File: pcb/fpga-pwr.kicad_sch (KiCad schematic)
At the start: 6 parts, among them M1V0 TestPoint, M1V2 TestPoint, U5 XC7A35T-FGG484

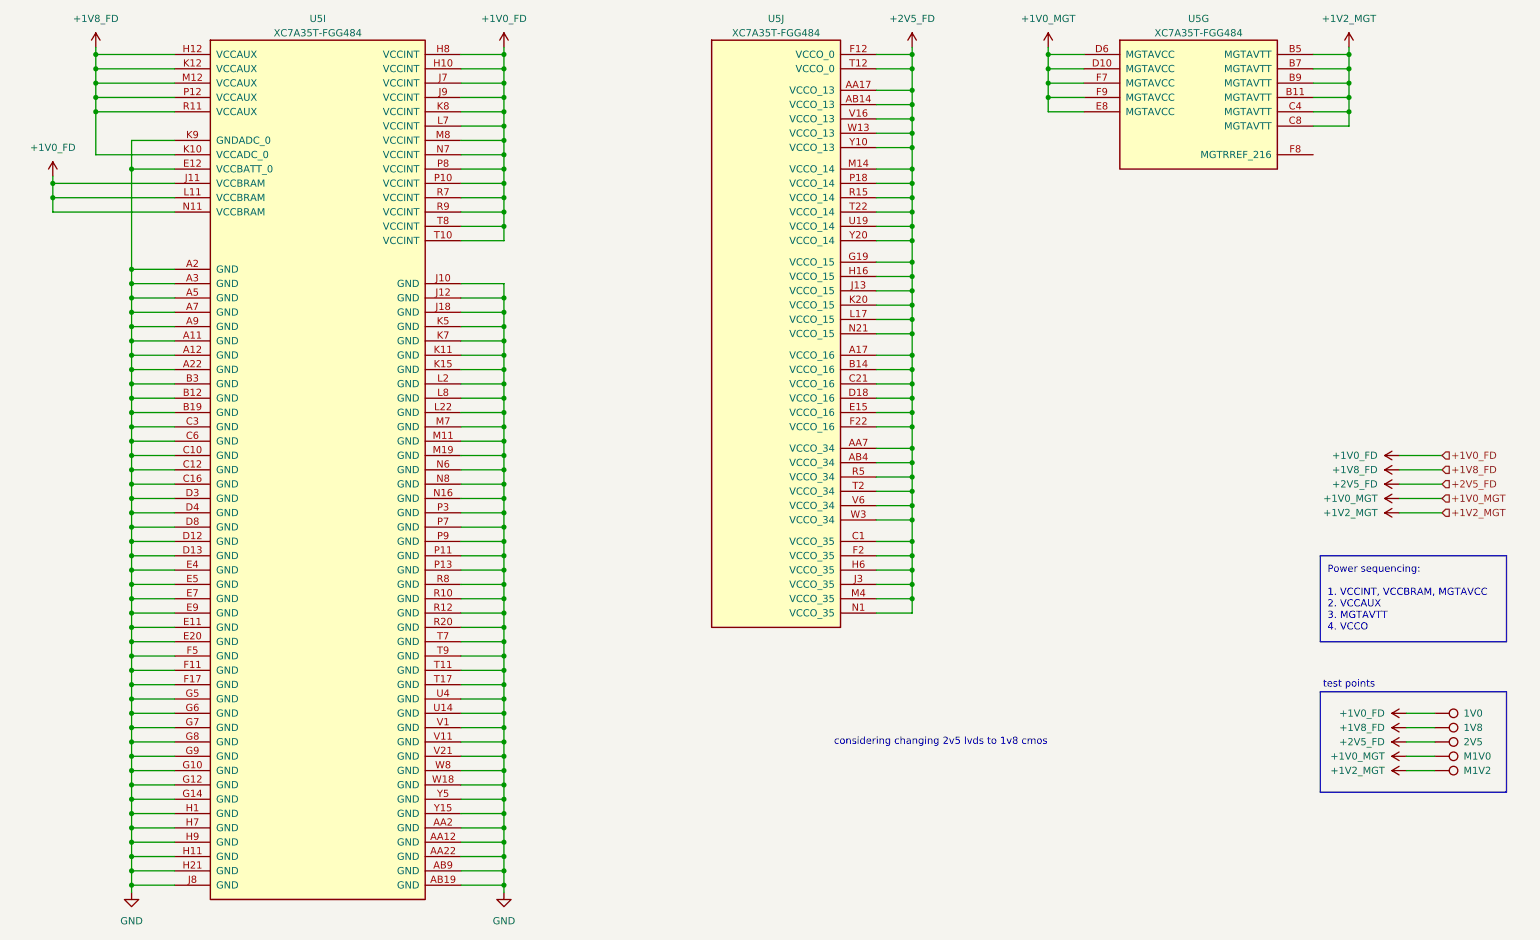
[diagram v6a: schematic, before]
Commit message: reorg hierarchical, define buses
added bus definitions, aliasing, reorganized sub-sheets for hierarchical interpretation, grouped fpga. pending dram and mram addition
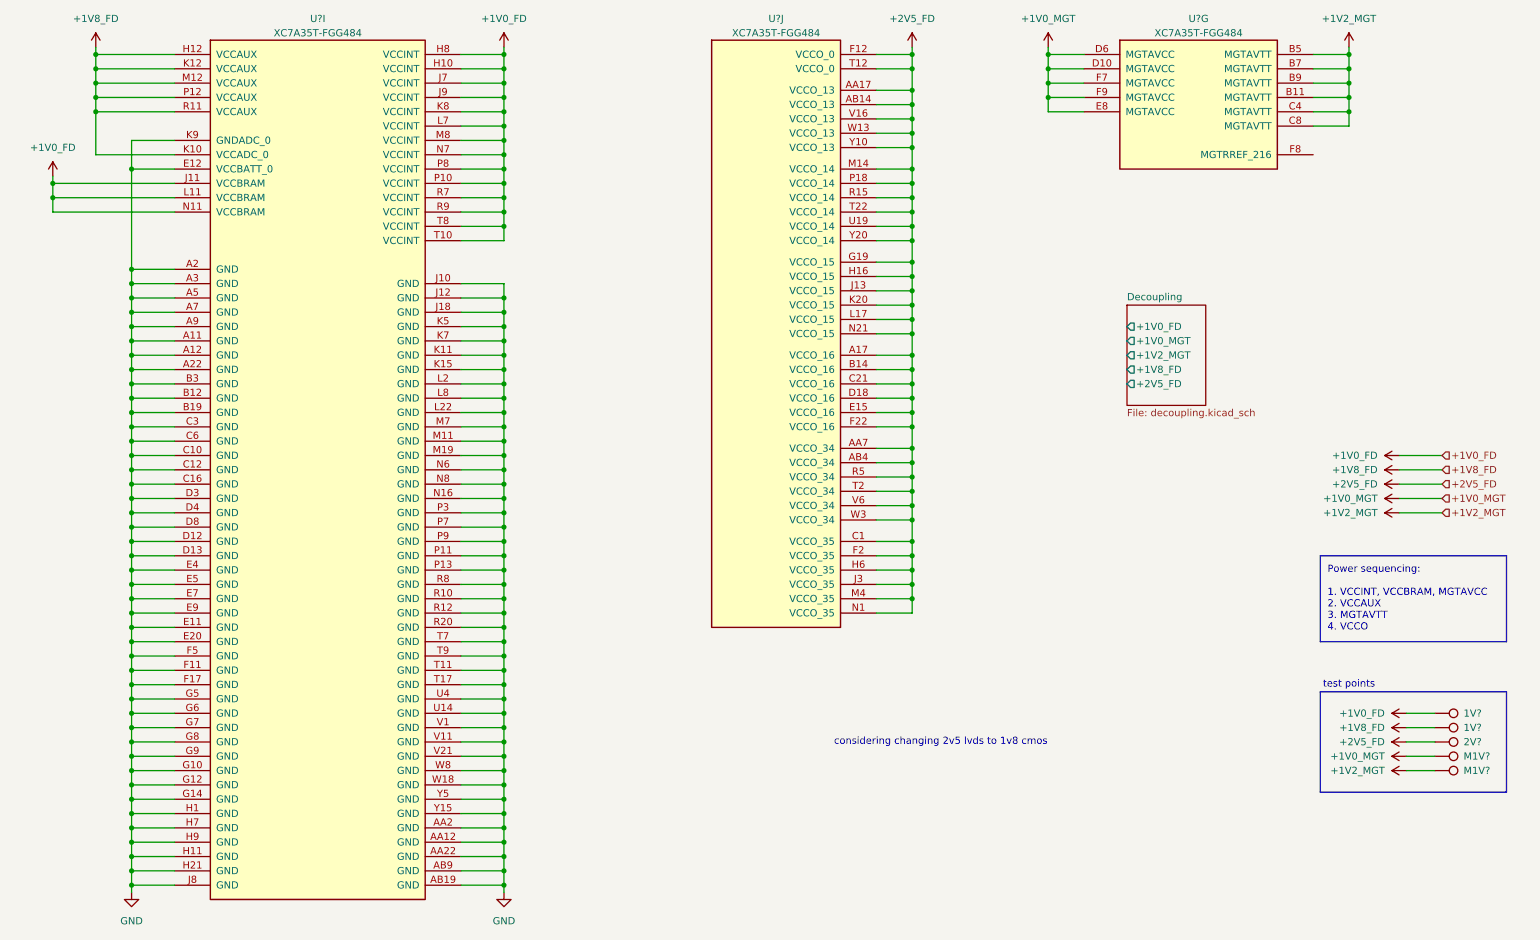
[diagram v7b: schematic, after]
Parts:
- renumbered 1V0 to 1V?, 1V8 to 1V?, 2V5 to 2V?, M1V2 to M1V?, M1V0 to M1V?, U5 to U?
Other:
- added sheet Decoupling (decoupling.kicad_sch)
